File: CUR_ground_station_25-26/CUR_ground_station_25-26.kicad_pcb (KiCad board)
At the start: 2 copper layers, 73.9 x 53.3 mm, 81 parts, among them J1 Conn_01x02, J2 UJ20-C-H-G-SMT-P16-TR, J3 Conn_Coaxial_Small, J4 Conn_01x04_Pin, Q1 NTR4003N, Q2 NTR4003N, SW1 PTS815SJM250SMTRLFS, SW2 PTS815SJM250SMTRLFS, SW3 PTS815SJM250SMTRLFS, SW4 PTS815SJM250SMTRLFS, SW5 PTS815SJM250SMTRLFS, SW7 PTS815SJM250SMTRLFS, SW8 PTS815SJM250SMTRLFS, U1 ESP32-S3-MINI-1, U2 BQ24232RGT, U3 NCP186AMX330TAG, U4 USBLC6-2SC6, U5 E22-400MM_22S, U6 2.13" Epaper Module

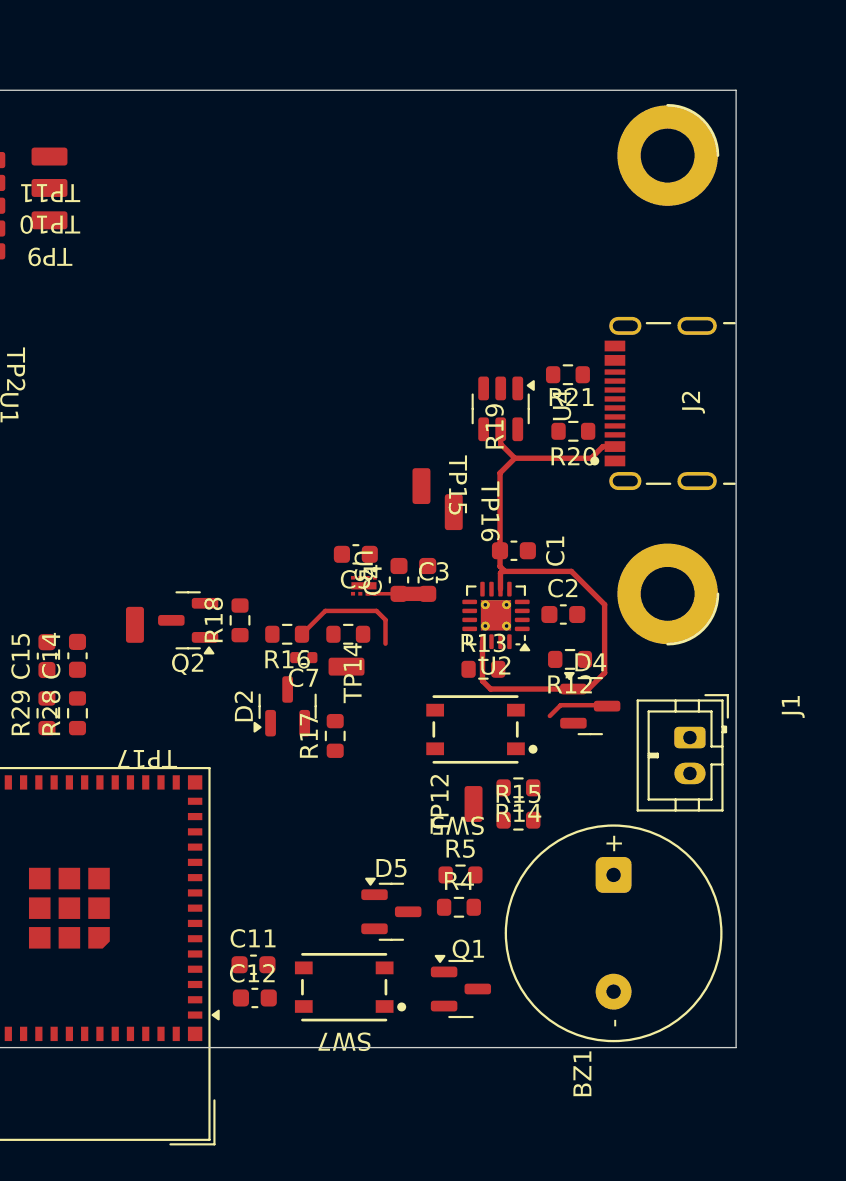
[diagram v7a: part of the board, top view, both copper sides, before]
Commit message: found decent power layout
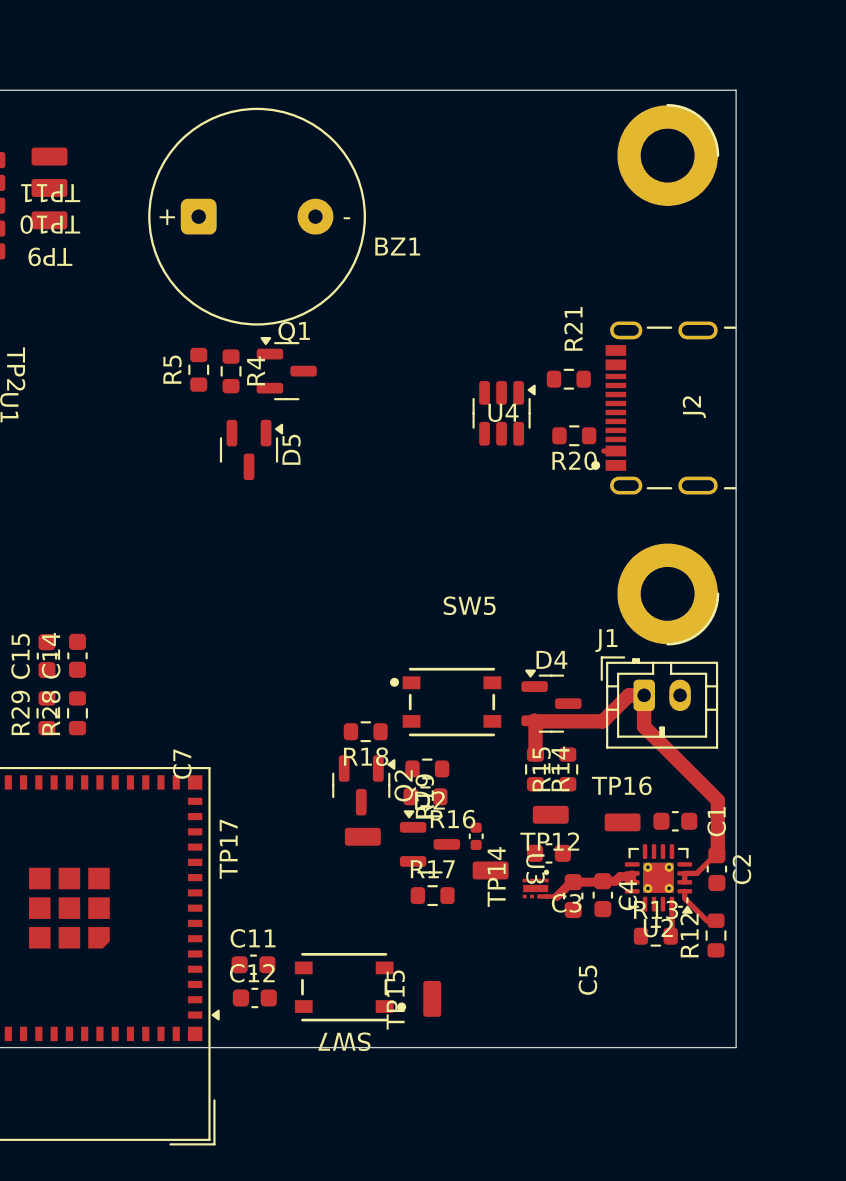
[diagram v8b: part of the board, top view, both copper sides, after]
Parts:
- moved BZ1 44.6 mm to (95.7, 57.0), turned to 0 degrees
- moved Q1 35.7 mm to (97.3, 65.7)
- moved R4 32.4 mm to (94.2, 65.7), turned to -90 degrees
- moved R5 31.7 mm to (92.5, 65.6), turned to 90 degrees
- moved TP15 28.6 mm to (105.5, 100.6), turned to 90 degrees
- moved D5 26.9 mm to (95.2, 70.0), turned to -90 degrees
- moved C4 20.9 mm to (115.0, 94.8), turned to -90 degrees
- moved C5 19.8 mm to (111.9, 92.5)
- moved TP16 19.7 mm to (116.1, 90.8), turned to 0 degrees
- moved U3 19.4 mm to (111.2, 94.5)
- moved C3 19.4 mm to (113.3, 94.9), turned to -90 degrees
- moved R13 17.7 mm to (117.9, 97.1)
- moved C1 17.5 mm to (119.0, 90.7)
- moved R12 17.4 mm to (121.2, 97.1), turned to 90 degrees
- moved TP17 17.3 mm to (101.6, 91.6), turned to 0 degrees
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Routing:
- net VBUS: track 35.4 -> 0.67 mm
- net +BATT: track 0.00 -> 21.9 mm
- net Net-(R16-Pad1): track 6.72 -> 0.00 mm
- net Net-(D4-Pad3): track 3.46 -> 0.00 mm
- net Net-(U2-TS): track 0.00 -> 2.65 mm
- net IN: track 3.35 -> 5.97 mm
- net Net-(U2-ISET): track 0.00 -> 1.82 mm
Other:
- copper layers 2 -> 4
